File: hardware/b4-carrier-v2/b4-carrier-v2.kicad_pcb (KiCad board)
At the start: 4 copper layers, 135 x 92 mm, 213 parts, among them J1 USB-C PD/CHARGE, J10 DEVKIT 3V3 ROW, J11 DEVKIT VIN ROW 22.86, J12 DEVKIT VIN ROW 25.40, J13 DEVKIT VIN ROW 27.94, J14 S3-ETH VBUS ROW, J15 S3-ETH IO20 ROW, J2 DC 6-20V, J20 BUTTONS, J21 TALLY, J22 EXT POT I, J23 EXT POT Z, J24 EXT POT F, J3 LENS, J4 ZOOM DEMAND, J5 FOCUS DEMAND, J6 OLED, Q1 AO3400A, Q2 AO3401A, Q3 AO3400A, Q4 AO3400A, Q5 AO3400A, Q6 AO3400A, U1 CH224A, U10 MCP4728, U11 ADS1115, U12 LM324, U13 CD4066B, U14 PC817, U2 BQ25798, U3 BQ29209, U4 TPS55340, U5 TPS259541, U6 INA219, U7 LM317, U8 AP63205, U9 AP2112K-3.3

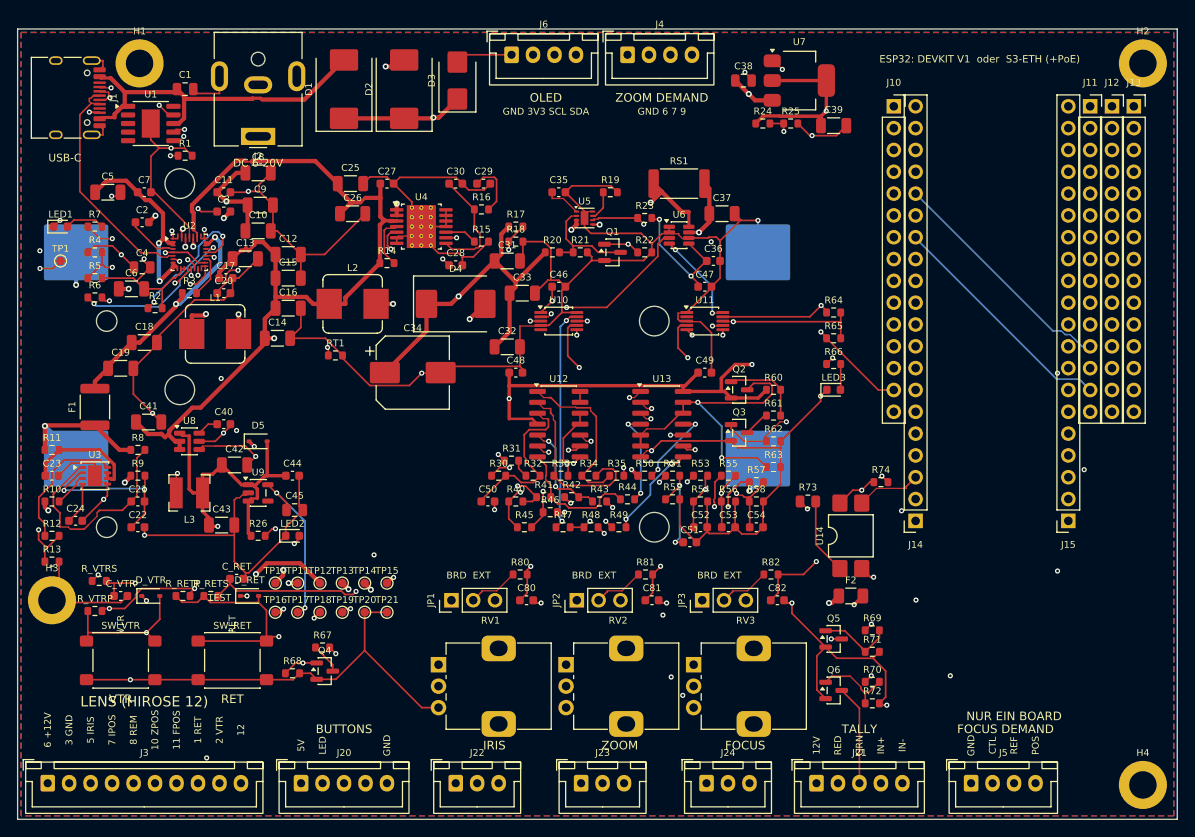
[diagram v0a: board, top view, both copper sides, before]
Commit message: Hardware: B4-Träger v2 – Leistungspfade, Abstände, Beschriftung (#120)
* Hardware B4-Traeger v2: Leistungspfade, Abstaende und Beschriftung

Breite Leistungspfade auf B.Cu (power_trunks.py) mit Via-Gruppen an den
Kondensatoren, von Hand gelegter Ladekern (BQ25798 gedreht, SW-Knoten direkt
zur Spule, PMID/SYS-Busse, PGND-Vias, PROG und LED am Pin), Via-Gruppen an
VBAT/CHG_IN des Laders und am eFuse-Eingang. fixup.py schliesst Freeroutings
Luecken mit eigenem Router, postprocess.py giesst Leistungsnetze breit,
naeht GND, misst Breiten und stellt Beschriftungen frei.
DRC: 0 offen, 0 Abstandsfehler, 0 Silk-Fehler.

Co-Authored-By: Claude Opus 5.5 <noreply@anthropic.com>

* B4-Traeger v2: __pycache__ ignorieren

Co-Authored-By: Claude Opus 5.5 <noreply@anthropic.com>

---------

Co-authored-by: Claude Opus 5.5 <noreply@anthropic.com>
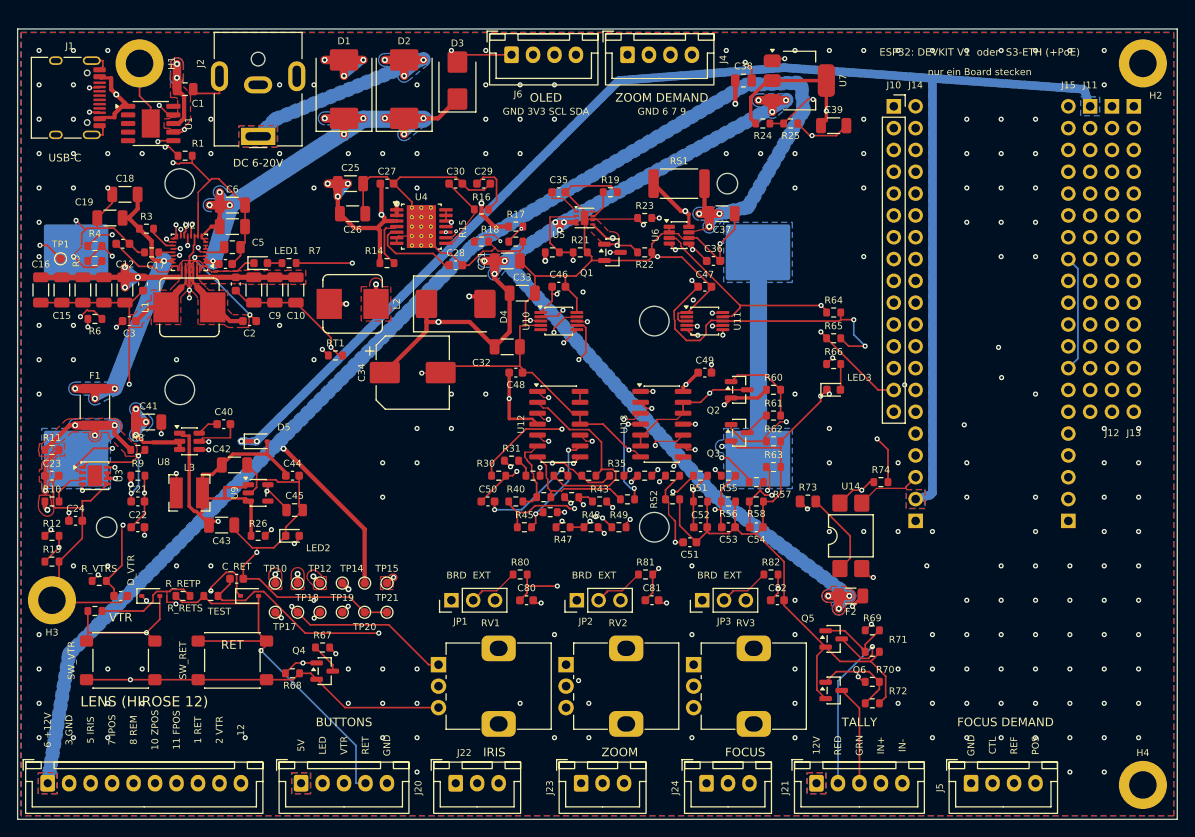
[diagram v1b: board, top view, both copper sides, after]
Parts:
- moved C16 28.9 mm to (2.70, 30.4), turned to -90 degrees
- moved C15 26.4 mm to (5.15, 30.4), turned to -90 degrees
- moved LED1 23.7 mm to (28.3, 27.2)
- moved C14 23.3 mm to (7.60, 30.4), turned to -90 degrees
- moved R7 23.0 mm to (31.6, 27.2), turned to 180 degrees
- moved C12 19.4 mm to (12.5, 30.4), turned to -90 degrees
- moved C19 17.5 mm to (10.8, 22.0), turned to 180 degrees
- moved C18 17.4 mm to (12.5, 19.2), turned to 180 degrees
- moved C2 17.0 mm to (27.0, 34.0), turned to 180 degrees
- moved C13 16.8 mm to (10.1, 30.4), turned to -90 degrees
- moved C3 16.8 mm to (13.0, 34.0)
- moved C6 15.3 mm to (25.0, 20.5)
- moved C5 15.0 mm to (25.0, 23.0)
- moved C8 13.6 mm to (27.5, 30.4), turned to -90 degrees
- moved C20 13.1 mm to (12.2, 25.0)
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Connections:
- J1 pad A6: DP -> (no net)
- J1 pad A7: DM -> (no net)
- J1 pad B6: DP -> (no net)
- J1 pad B7: DM -> (no net)
- U2 pad 6: DP -> CHG_DPDM
- U2 pad 7: DM -> CHG_DPDM
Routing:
- net V12_LENS: track 129.6 -> 178.8 mm, vias 2 -> 4
- net GND: track 1158.8 -> 1123.9 mm, vias 21 -> 214
- net ESP_5V: track 141.1 -> 175.3 mm, vias 1 -> 2
- net VSYS: track 134.3 -> 164.5 mm, vias 2 -> 12
- net DP: track 27.9 -> 0.00 mm
- net DM: track 26.3 -> 0.00 mm, vias 2 -> 0
- net VBAT: track 72.3 -> 95.8 mm, vias 3 -> 5
- net V12: track 191.3 -> 213.7 mm, vias 5 -> 17
- net USB_VBUS: track 41.5 -> 61.5 mm, vias 0 -> 6
- net ZOOM_POS: track 97.6 -> 81.6 mm, vias 2 -> 1
- net PROG: track 17.0 -> 1.68 mm, vias 2 -> 0
- net A3V3: track 368.2 -> 383.2 mm, vias 12 -> 13
- net DC_IN: track 20.7 -> 35.3 mm, vias 1 -> 3
- net IRIS_POS: track 96.5 -> 82.7 mm, vias 2 -> 1
- net FOCUS_POS: track 97.9 -> 84.8 mm, vias 2 -> 1
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- added copper zone on F.Cu, net BAL_VDD
- added copper zone on In1.Cu, net BAL_VDD
- added copper zone on F.Cu, net BST_SW
- added copper zone on In1.Cu, net BST_SW
- added copper zone on B.Cu, net CHG_IN
- added copper zone on F.Cu, net CHG_IN
- added copper zone on In1.Cu, net CHG_IN
- added copper zone on B.Cu, net DC_IN
- added copper zone on F.Cu, net DC_IN
- added copper zone on In1.Cu, net DC_IN
- added copper zone on In2.Cu, net DC_IN
- added copper zone on B.Cu, net ESP_5V
- added copper zone on F.Cu, net ESP_5V
- added copper zone on In1.Cu, net ESP_5V
- added copper zone on In2.Cu, net ESP_5V
- added copper zone on F.Cu, net PMID
- added copper zone on F.Cu, net SW1
- added copper zone on F.Cu, net SW2
- added copper zone on B.Cu, net TALLY_V
- added copper zone on F.Cu, net TALLY_V
- added copper zone on In1.Cu, net TALLY_V
- added copper zone on In2.Cu, net TALLY_V
- added copper zone on B.Cu, net USB_VBUS
- added copper zone on F.Cu, net USB_VBUS
- added copper zone on In2.Cu, net USB_VBUS
- added copper zone on B.Cu, net V12
- added copper zone on F.Cu, net V12
- added copper zone on In1.Cu, net V12
- added copper zone on F.Cu, net V12E
- added copper zone on In2.Cu, net V12E
- added copper zone on B.Cu, net V12_LENS
- added copper zone on F.Cu, net V12_LENS
- added copper zone on In1.Cu, net V12_LENS
- added copper zone on In2.Cu, net V12_LENS
- added copper zone on B.Cu, net V5
- added copper zone on F.Cu, net V5
- added copper zone on In1.Cu, net V5
- added copper zone on In2.Cu, net V5
- added copper zone on F.Cu, net V9
- added copper zone on In1.Cu, net V9
- added copper zone on In2.Cu, net V9
- added copper zone on B.Cu, net VBAT
- added copper zone on F.Cu, net VBAT
- added copper zone on In1.Cu, net VBAT
- added copper zone on B.Cu, net VBAT_RAW
- added copper zone on F.Cu, net VBAT_RAW
- added copper zone on B.Cu, net VMID
- added copper zone on F.Cu, net VMID
- added copper zone on In1.Cu, net VMID
- added copper zone on In2.Cu, net VMID
- added copper zone on B.Cu, net VSYS
- added copper zone on F.Cu, net VSYS
- added copper zone on In1.Cu, net VSYS
- added copper zone on In2.Cu, net VSYS
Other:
- board text added: "nur ein Board stecken"
- board text removed: "NUR EIN BOARD"
